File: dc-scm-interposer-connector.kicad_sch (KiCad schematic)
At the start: 0 parts

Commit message: [#103224] Add dc-scm interposer connectors, fix typo in JTAG nametags
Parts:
- added J2001, J2002: PinSocket_2x10_P2.54mm_SMD, antmicro-footprints:PinSocket_2x10_P2.54mm_SMD, symbol Antmicro Symbols:PinSocket_2x10_P2.54mm_SMD
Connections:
- new net DC_SCM_12V_AUX: J2001.15
- new net EC_ESPI.IO0: J2001.7
- new net EC_ESPI.IO1: J2001.2
- new net EC_ESPI.IO3: J2001.6
- new net EC_ESPI.SCK: J2001.1
- new net EC_ESPI.~{ALERT0}: J2001.8
- new net EC_ESPI.~{CS0}: J2001.3
- new net EC_ESPI.~{RESET}: J2001.5
- new net EC_SCM_ESPI.IO2: J2001.4
- new net GND: J2001.10, J2001.11, J2001.9
- no-connect marks 0 -> 8
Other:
- note added: "DC-SCM Interposer Connectors"
- note added: "Not connected to anything Used only for mechanical purposes!"
- note added: "TODO: Decide how many additional, disconnected connectors are needed for mechanical stability"

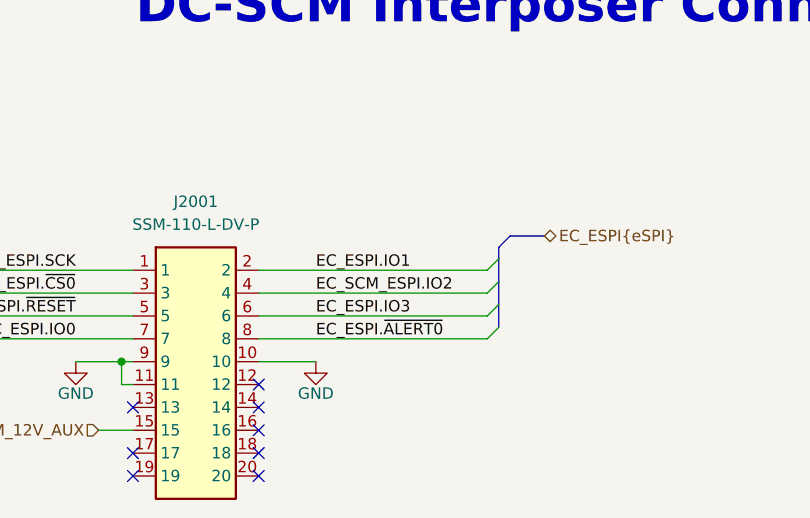
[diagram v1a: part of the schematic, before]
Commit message: [#103224] Add MEC1723 IC, JTAG connections, eSPI connections, QSPI connections, fix typo in UART
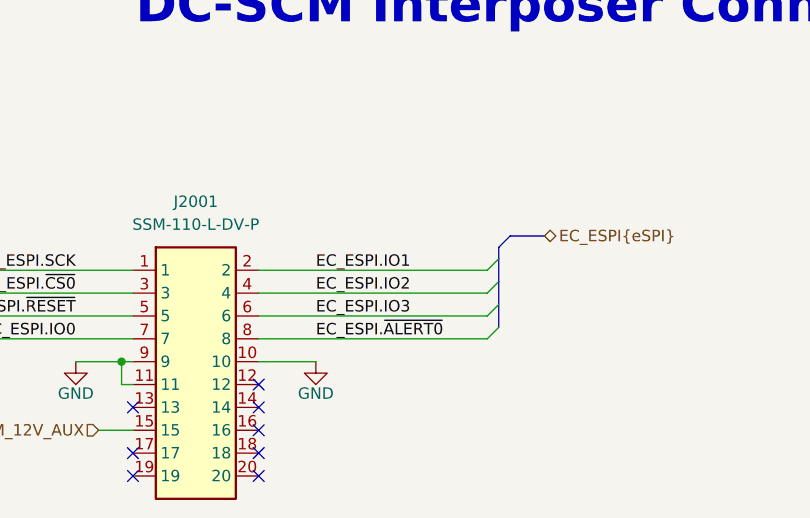
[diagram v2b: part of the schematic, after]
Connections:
- net EC_SCM_ESPI.IO2 renamed EC_ESPI.IO2
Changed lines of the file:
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@@
 		)
 	)
-	(label "EC_SCM_ESPI.IO2"
+	(label "EC_ESPI.IO2"
 		(at 118.11 95.25 0)
 		(effects
@@
 		)
 	)
+	(netclass_flag ""
+		(length 2.54)
+		(shape round)
+		(at 73.66 92.71 90)
+		(effects
+			(font
+				(size 1.27 1.27)
+			)
+			(justify left bottom)
+		)
+		(property "Netclass" "50Ohm-se"
+			(at 70.104 92.71 0)
+			(show_name no)
+			(do_not_autoplace no)
+			(effects
+				(font
+					(size 1.27 1.27)
+				)
+				(justify right)
+			)
+		)
+		(property "Component Class" ""
+			(at -125.73 215.9 0)
+			(show_name no)
+			(do_not_autoplace no)
+			(effects
+				(font
+					(size 1.27 1.27)
+					(italic yes)
+				)
+				(justify right)
+			)
+		)
+	)

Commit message: [#103224] Add decoupling, add reset, add notes
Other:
- note added: "Mounted on the bottom side - remember about proper orientation!"
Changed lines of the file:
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@@
+		)
+	)
+	(text "Mounted on the bottom side - remember about proper orientation!"
+		(exclude_from_sim no)
+		(at 106.172 124.714 0)
+		(effects
+			(font
+				(size 1.27 1.27)
+				(color 255 35 71 1)
+			)
 		)
 	)

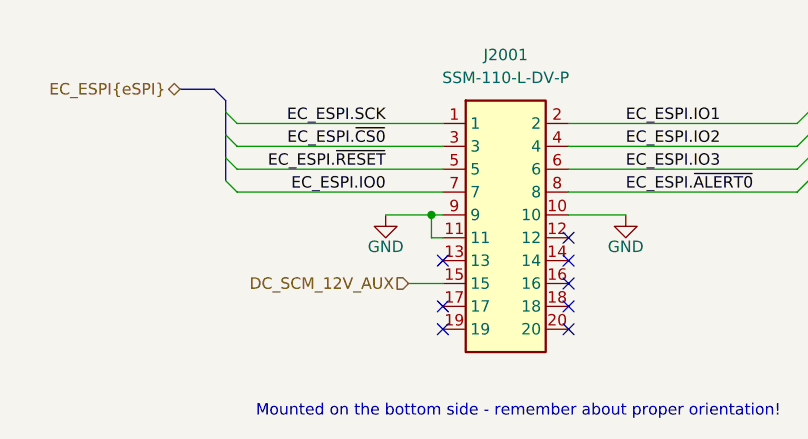
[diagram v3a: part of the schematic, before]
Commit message: [#103224] Add 7-segment display section, add battery cicruit
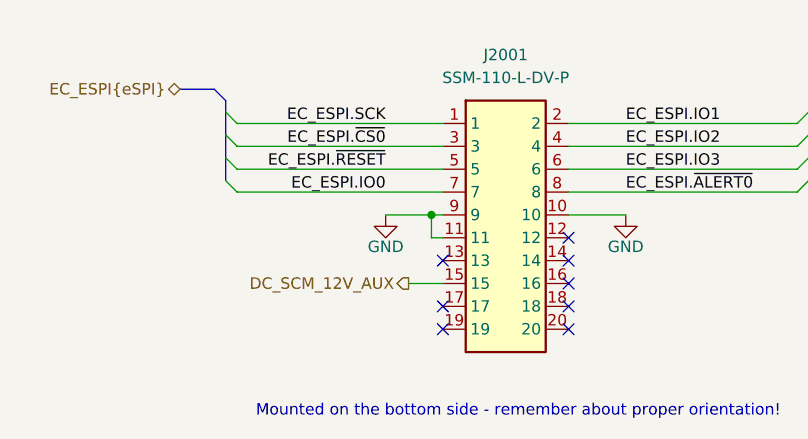
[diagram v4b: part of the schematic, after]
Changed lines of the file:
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@@
 	)
 	(hierarchical_label "DC_SCM_12V_AUX"
-		(shape input)
+		(shape output)
 		(at 93.98 110.49 180)
 		(effects

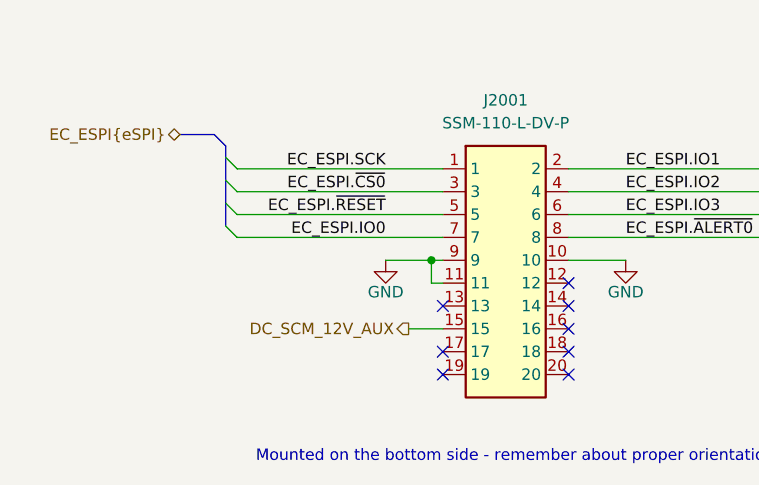
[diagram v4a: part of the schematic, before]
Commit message: [#103224] Change buffer ICs, change JTAG connector, move BSS_STRAP resistors to MEC1723 sheet
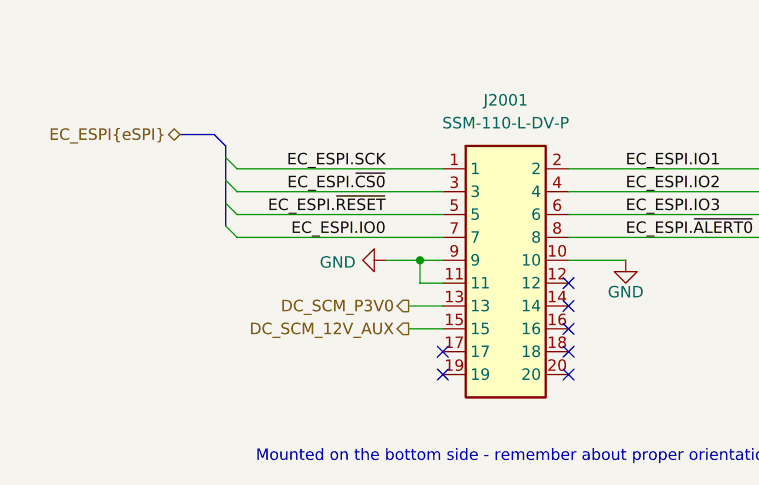
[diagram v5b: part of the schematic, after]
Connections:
- net DC_SCM_P3V0: now reaches J2001.13
- no-connect marks 8 -> 7
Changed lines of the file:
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@@
 	)
 	(junction
-		(at 96.52 102.87)
+		(at 95.25 102.87)
 		(diameter 0)
 		(color 0 0 0 0)
@@
 	)
 	(no_connect
-		(at 97.79 107.95)
-	)
-	(no_connect
 		(at 111.76 113.03)
 	)
@@
 		)
 	)
-	(wire
-		(pts
-			(xy 91.44 102.87) (xy 96.52 102.87)
-		)
-		(stroke
-			(width 0)
-			(type default)
-		)
-	)
 	(bus
 		(pts
@@
 		)
 	)
-	(wire
-		(pts
-			(xy 96.52 105.41) (xy 96.52 102.87)
-		)
-		(stroke
-			(width 0)
-			(type default)
-		)
-	)
 	(bus
 		(pts
@@
 	(wire
 		(pts
+			(xy 95.25 105.41) (xy 95.25 102.87)
+		)
+		(stroke
+			(width 0)
+			(type default)
+		)
+	)
+	(wire
+		(pts
+			(xy 93.98 107.95) (xy 97.79 107.95)
+		)
+		(stroke
+			(width 0)
+			(type default)
+		)
+	)
+	(wire
+		(pts
+			(xy 95.25 102.87) (xy 97.79 102.87)
+		)
+		(stroke
+			(width 0)
+			(type default)
+		)
+	)
+	(wire
+		(pts
 			(xy 74.93 92.71) (xy 97.79 92.71)
 		)
@@
 		)
 	)
-	(wire
-		(pts
-			(xy 97.79 105.41) (xy 96.52 105.41)
-		)
-		(stroke
-			(width 0)
-			(type default)
-		)
-	)
 	(bus
 		(pts
@@
 	(wire
 		(pts
-			(xy 96.52 102.87) (xy 97.79 102.87)
+			(xy 91.44 102.87) (xy 95.25 102.87)
 		)
 		(stroke
@@
 		(pts
 			(xy 111.76 97.79) (xy 137.16 97.79)
+		)
+		(stroke
+			(width 0)
+			(type default)
+		)
+	)
+	(wire
+		(pts
+			(xy 97.79 105.41) (xy 95.25 105.41)
 		)
 		(stroke
@@
 			)
 			(justify left)
+		)
+	)
+	(hierarchical_label "DC_SCM_P3V0"
+		(shape output)
+		(at 93.98 107.95 180)
+		(effects
+			(font
+				(size 1.27 1.27)
+			)
+			(justify right)
 		)
 	)
@@
 	(symbol
 		(lib_id "antmicropower:GND")
-		(at 91.44 102.87 0)
+		(at 91.44 102.87 270)
 		(unit 1)
 		(body_style 1)
@@
 		(dnp no)
 		(property "Reference" "#PWR02002"
-			(at 100.33 105.41 0)
+			(at 88.9 111.76 0)
 			(hide yes)
 			(show_name no)
@@
 		)
 		(property "Value" "GND"
-			(at 91.44 105.664 0)
+			(at 86.106 102.362 90)
 			(show_name no)
 			(do_not_autoplace no)
@@
 		)
 		(property "Footprint" ""
-			(at 100.33 110.49 0)
+			(at 83.82 111.76 0)
 			(hide yes)
 			(show_name no)
@@
 		)
 		(property "Datasheet" ""
-			(at 100.33 115.57 0)
+			(at 78.74 111.76 0)
 			(hide yes)
 			(show_name no)
@@
 		)
 		(property "Description" ""
-			(at 100.33 118.11 0)
+			(at 76.2 111.76 0)
 			(hide yes)
 			(show_name no)
@@
 		)
 		(property "Author" "Antmicro"
-			(at 100.33 110.49 0)
+			(at 83.82 111.76 0)
 			(hide yes)
 			(show_name no)
@@
 		)
 		(property "License" "Apache-2.0"
-			(at 100.33 113.03 0)
-			(hide yes)
-			(show_name no)
+			(at 81.28 111.76 0)
+			(hide yes)
+			(show_name no)

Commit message: [#103224] Divide 7SEG bus into 2, rename JTAG connector pins
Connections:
- net DC_SCM_STBY_EN: now reaches J2001.16
- no-connect marks 7 -> 6
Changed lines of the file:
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@@
 			(font
 				(size 1.27 1.27)
-				(color 255 52 75 1)
 			)
 		)
@@
 			(font
 				(size 1.27 1.27)
-				(color 255 35 71 1)
 			)
 		)
@@
 	(text "Not connected to anything\nUsed only for mechanical purposes!"
 		(exclude_from_sim no)
-		(at 222.758 97.028 0)
+		(at 223.012 100.076 0)
 		(effects
 			(font
@@
 	)
 	(no_connect
-		(at 111.76 110.49)
-	)
-	(no_connect
 		(at 111.76 105.41)
 	)
@@
 		)
 	)
+	(hierarchical_label "DC_SCM_STBY_EN"
+		(shape output)
+		(at 111.76 110.49 0)
+		(effects
+			(font
+				(size 1.27 1.27)
+			)
+			(justify left)
+		)
+	)

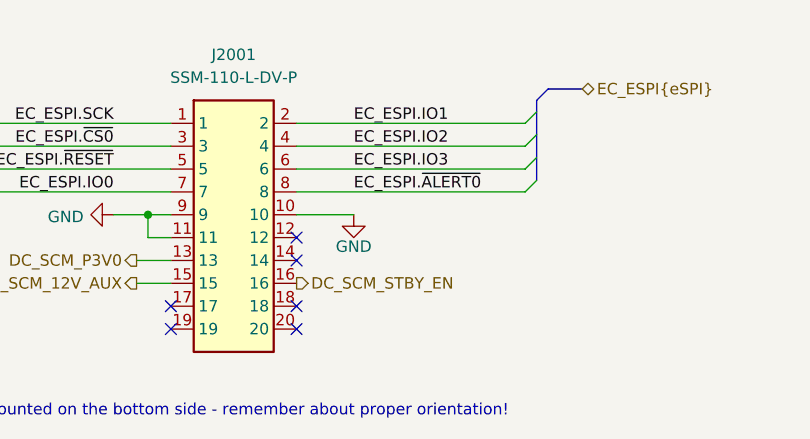
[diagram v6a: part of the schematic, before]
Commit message: [#103224] Add crucial signals, add strapping
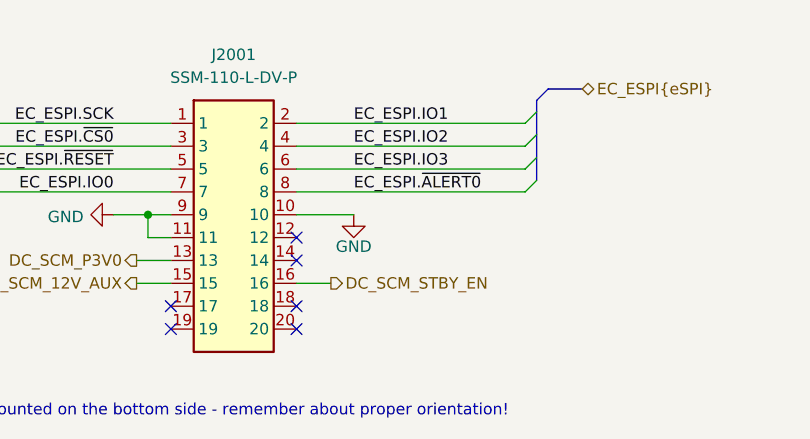
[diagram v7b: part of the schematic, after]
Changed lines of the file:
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@@
+	(wire
+		(pts
+			(xy 115.57 110.49) (xy 111.76 110.49)
+		)
+		(stroke
+			(width 0)
+			(type default)
+		)
+	)
 	(wire
 		(pts
@@
 	(hierarchical_label "DC_SCM_STBY_EN"
 		(shape output)
-		(at 111.76 110.49 0)
-		(effects
-			(font
+		(at 115.57 110.49 0)
+		(effects
+			(font

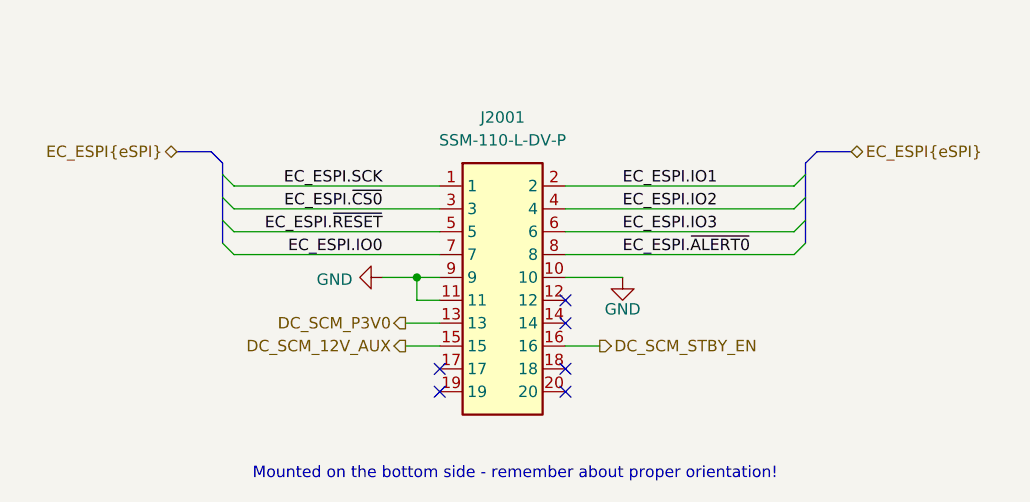
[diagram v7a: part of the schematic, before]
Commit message: [#103224] Add UART1, added GND to breakout connectors, fix orientation of DC-SCM connector, delete unused notes
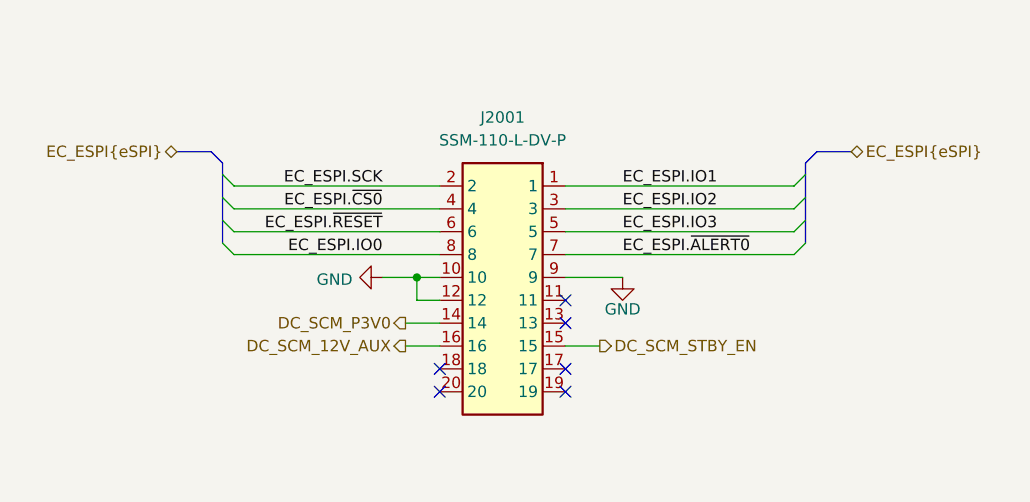
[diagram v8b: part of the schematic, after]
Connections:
- net DC_SCM_12V_AUX: now also J2001.16; no longer J2001.15
- net DC_SCM_P3V0: now also J2001.14; no longer J2001.13
- net DC_SCM_STBY_EN: now also J2001.15; no longer J2001.16
- net EC_ESPI.IO0: now also J2001.8; no longer J2001.7
- net EC_ESPI.IO1: now also J2001.1; no longer J2001.2
- net EC_ESPI.IO2: now also J2001.3; no longer J2001.4
- net EC_ESPI.IO3: now also J2001.5; no longer J2001.6
- net EC_ESPI.SCK: now also J2001.2; no longer J2001.1
- net EC_ESPI.~{ALERT0}: now also J2001.7; no longer J2001.8
- net EC_ESPI.~{CS0}: now also J2001.4; no longer J2001.3
- net EC_ESPI.~{RESET}: now also J2001.6; no longer J2001.5
- net GND: now also J2001.12; no longer J2001.11
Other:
- note removed: "Mounted on the bottom side - remember about proper orientation!"
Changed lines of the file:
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@@
-		)
-	)
-	(text "Mounted on the bottom side - remember about proper orientation!"
-		(exclude_from_sim no)
-		(at 106.172 124.714 0)
-		(effects
-			(font
-				(size 1.27 1.27)
-			)
 		)
 	)
@@
 	)
 	(symbol
+		(lib_id "Antmicro Symbols:PinSocket_2x10_P2.54mm_SMD")
+		(at 111.76 92.71 0)
+		(mirror y)
+		(unit 1)
+		(body_style 1)
+		(exclude_from_sim no)
+		(in_bom yes)
+		(on_board yes)
+		(in_pos_files yes)
+		(dnp no)
+		(property "Reference" "J2001"
+			(at 104.775 85.09 0)
+			(show_name no)
+			(do_not_autoplace no)
+			(effects
+				(font
+					(size 1.27 1.27)
+					(thickness 0.15)
+				)
+			)
+		)
+		(property "Value" "PinSocket_2x10_P2.54mm_SMD"
+			(at 83.82 100.33 0)
+			(hide yes)
+			(show_name no)
+			(do_not_autoplace no)
+			(effects
+				(font
+					(size 1.27 1.27)
+					(thickness 0.15)
+				)
+				(justify left bottom)
+			)
+		)
+		(property "Footprint" "antmicro-footprints:PinSocket_2x10_P2.54mm_SMD"
+			(at 83.82 102.87 0)
+			(hide yes)
+			(show_name no)
+			(do_not_autoplace no)
+			(effects
+				(font
+					(size 1.27 1.27)
+					(thickness 0.15)
+				)
+				(justify left bottom)
+			)
+		)
+		(property "Datasheet" "https://eu.mouser.com/datasheet/2/527/ssm_sm-2853675.pdf"
+			(at 83.82 105.41 0)
+			(hide yes)
+			(show_name no)
+			(do_not_autoplace no)
+			(effects
+				(font
+					(size 1.27 1.27)
+					(thickness 0.15)
+				)
+				(justify left bottom)
+			)
+		)
+		(property "Description" "PCB Receptacle, Board-to-Board, 2.54 mm, 2 Rows, 20 Contacts, Surface Mount"
+			(at 83.82 115.57 0)
+			(hide yes)
+			(show_name no)
+			(do_not_autoplace no)
+			(effects
+				(font
+					(size 1.27 1.27)
+				)
+				(justify left bottom)
+			)
+		)
+		(property "MPN" "SSM-110-L-DV-P"
+			(at 104.775 87.63 0)
+			(show_name no)
+			(do_not_autoplace no)
+			(effects
+				(font
+					(size 1.27 1.27)
+					(thickness 0.15)
+				)
+			)
+		)
+		(property "Manufacturer" "Samtec"
+			(at 83.82 107.95 0)
+			(hide yes)
+			(show_name no)
+			(do_not_autoplace no)
+			(effects
+				(font
+					(size 1.27 1.27)
+					(thickness 0.15)
+				)
+				(justify left bottom)
+			)
+		)
+		(property "Author" "Antmicro"
+			(at 83.82 110.49 0)
+			(hide yes)
+			(show_name no)
+			(do_not_autoplace no)
+			(effects
+				(font
+					(size 1.27 1.27)
+					(thickness 0.15)
+				)
+				(justify left bottom)
+			)
+		)
+		(property "License" "Apache-2.0"
+			(at 83.82 113.03 0)
+			(hide yes)
+			(show_name no)
+			(do_not_autoplace no)
+			(effects
+				(font
+					(size 1.27 1.27)
+					(thickness 0.15)
+				)
+				(justify left bottom)
+			)
+		)
+		(pin "7"
+		)
+		(pin "19"
+		)
+		(pin "18"
+		)
+		(pin "9"
+		)
+		(pin "10"
+		)
+		(pin "8"
+		)
+		(pin "15"
+		)
+		(pin "14"
+		)
+		(pin "13"
+		)
+		(pin "11"
+		)
+		(pin "12"
+		)
+		(pin "17"
+		)
+		(pin "20"
+		)
+		(pin "6"
+		)
+		(pin "3"
+		)
+		(pin "5"
+		)
+		(pin "16"
+		)
+		(pin "4"
+		)
+		(pin "2"
+		)
+		(pin "1"
+		)
+		(instances
+			(project "dc-scm-server-integration-espi-adapter"
+				(path "/df391740-647e-4ab6-9dcd-d61184d66fe9/dad11b40-64da-40df-af81-feff62248020"
+					(reference "J2001")
+					(unit 1)
+				)
+			)
+		)
+	)
+	(symbol
 		(lib_id "antmicropower:GND")
 		(at 91.44 102.87 270)
@@
 					(unit 1)
 				)
-			)
-		)
-	)
-	(symbol
-		(lib_id "Antmicro Symbols:PinSocket_2x10_P2.54mm_SMD")
-		(at 97.79 92.71 0)
-		(unit 1)
-		(body_style 1)
-		(exclude_from_sim no)
-		(in_bom yes)
-		(on_board yes)
-		(in_pos_files yes)
-		(dnp no)
-		(fields_autoplaced yes)
-		(property "Reference" "J2001"
-			(at 104.775 85.09 0)
-			(show_name no)
-			(do_not_autoplace no)
-			(effects
-				(font
-					(size 1.27 1.27)
-					(thickness 0.15)
-				)
-			)
-		)
-		(property "Value" "PinSocket_2x10_P2.54mm_SMD"
-			(at 125.73 100.33 0)
-			(hide yes)
-			(show_name no)
-			(do_not_autoplace no)
-			(effects
-				(font
-					(size 1.27 1.27)
-					(thickness 0.15)
-				)
-				(justify left bottom)
-			)
-		)
-		(property "Footprint" "antmicro-footprints:PinSocket_2x10_P2.54mm_SMD"
-			(at 125.73 102.87 0)
-			(hide yes)
-			(show_name no)
-			(do_not_autoplace no)
-			(effects
-				(font
-					(size 1.27 1.27)
-					(thickness 0.15)
-				)
-				(justify left bottom)
-			)
-		)
-		(property "Datasheet" "https://eu.mouser.com/datasheet/2/527/ssm_sm-2853675.pdf"
-			(at 125.73 105.41 0)
-			(hide yes)
-			(show_name no)
-			(do_not_autoplace no)
-			(effects
-				(font
-					(size 1.27 1.27)
-					(thickness 0.15)
-				)
-				(justify left bottom)
-			)
-		)
-		(property "Description" "PCB Receptacle, Board-to-Board, 2.54 mm, 2 Rows, 20 Contacts, Surface Mount"
-			(at 125.73 115.57 0)
-			(hide yes)
-			(show_name no)
-			(do_not_autoplace no)
-			(effects
-				(font
-					(size 1.27 1.27)
-				)
-				(justify left bottom)
-			)
-		)
-		(property "MPN" "SSM-110-L-DV-P"
-			(at 104.775 87.63 0)
-			(show_name no)
-			(do_not_autoplace no)
-			(effects
-				(font
-					(size 1.27 1.27)
-					(thickness 0.15)
-				)
-			)
-		)
-		(property "Manufacturer" "Samtec"
-			(at 125.73 107.95 0)
-			(hide yes)
-			(show_name no)
-			(do_not_autoplace no)
-			(effects
-				(font
-					(size 1.27 1.27)
-					(thickness 0.15)
-				)
-				(justify left bottom)
-			)
-		)
-		(property "Author" "Antmicro"
-			(at 125.73 110.49 0)
-			(hide yes)
-			(show_name no)
-			(do_not_autoplace no)
-			(effects
-				(font
-					(size 1.27 1.27)
-					(thickness 0.15)
-				)
-				(justify left bottom)
-			)
-		)
-		(property "License" "Apache-2.0"
-			(at 125.73 113.03 0)
-			(hide yes)
-			(show_name no)
-			(do_not_autoplace no)
-			(effects
-				(font
-					(size 1.27 1.27)
-					(thickness 0.15)
-				)
-				(justify left bottom)
-			)
-		)
-		(pin "7"
-		)
-		(pin "19"
-		)
-		(pin "18"
-		)
-		(pin "9"
-		)
-		(pin "10"
-		)
-		(pin "8"
-		)
-		(pin "15"
-		)
-		(pin "14"
-		)
-		(pin "13"
-		)
-		(pin "11"
-		)
-		(pin "12"
-		)
-		(pin "17"
-		)
-		(pin "20"
-		)
-		(pin "6"
-		)
-		(pin "3"
-		)
-		(pin "5"
-		)
-		(pin "16"
-		)
-		(pin "4"
-		)
-		(pin "2"
-		)
-		(pin "1"
-		)
-		(instances
-			(project "dc-scm-server-integration-espi-adapter"
-				(path "/df391740-647e-4ab6-9dcd-d61184d66fe9/dad11b40-64da-40df-af81-feff62248020"
-					(reference "J2001")
-					(unit 1)
-				)
